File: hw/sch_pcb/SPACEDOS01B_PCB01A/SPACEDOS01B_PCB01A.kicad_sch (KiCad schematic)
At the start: 53 parts, among them M1 HOLE, M10 BMI-S-204-F, M2 HOLE, M3 HOLE, M4 HOLE, M6 BMI-S-210-F, M8 BMI-S-204-F, M9 BMI-S-204-F, U1 OPA2314, U2 OPA2314, U3 ISL21080DIH312Z-TK 1V25, U4 TS7211, U5 TS5A4594

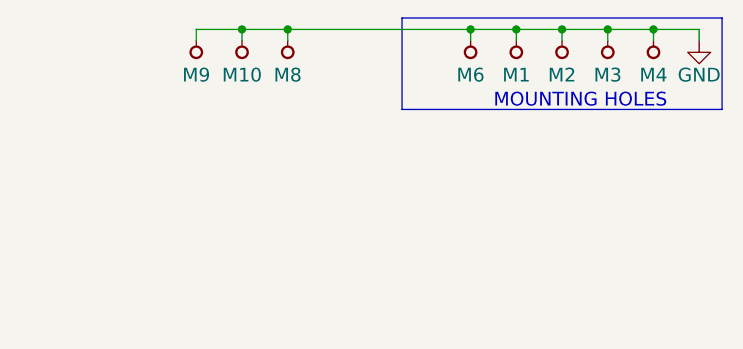
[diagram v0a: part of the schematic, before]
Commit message: Update designs to KiCAD 6. Update schematics datasheet links Minor schematics improvements (titleblocks, schematics layout)
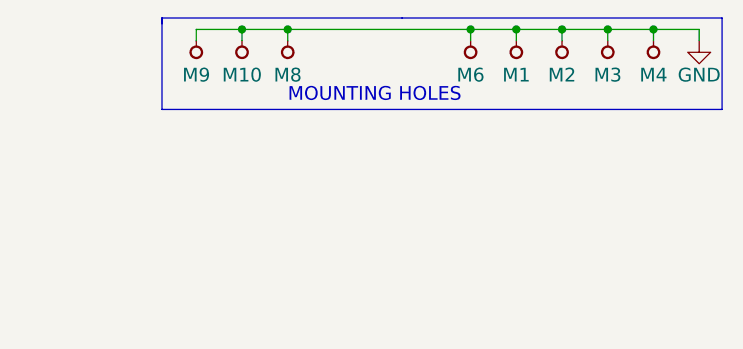
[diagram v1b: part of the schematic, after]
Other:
- company: Universal Scientific \nTechnologies s.r.o.  -> www.ust.cz
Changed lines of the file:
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@@
   (title_block
     (title "SPACEDOS01B")
-    (date "%F")
-    (company "Universal Scientific \\nTechnologies s.r.o. ")
+    (date "2023-01-26")
+    (company "www.ust.cz")
+    (comment 1 "Semiconductor \\nIonizing radiation \\nsatellite spectrometer  \\nand dosimeter ")
+    (comment 3 "Universal Scientific Technologies s.r.o. ")
   )
   (junction (at 46.99 24.13) (diameter 0) (color 0 0 0 0)
@@
     (stroke (width 0) (type default) (color 0 0 0 0))
   )
+  (polyline (pts (xy 219.71 15.24) (xy 219.71 15.875))
+    (stroke (width 0) (type default) (color 0 0 0 0))
+  )
   (wire (pts (xy 143.51 130.81) (xy 142.24 130.81))
     (stroke (width 0) (type default) (color 0 0 0 0))
@@
     (stroke (width 0) (type default) (color 0 0 0 0))
   )
-  (polyline (pts (xy 246.38 15.24) (xy 246.38 25.4))
+  (polyline (pts (xy 219.71 15.24) (xy 219.71 25.4))
     (stroke (width 0) (type default) (color 0 0 0 0))
   )
@@
     (stroke (width 0) (type default) (color 0 0 0 0))
   )
+  (polyline (pts (xy 246.38 15.24) (xy 219.71 15.24))
+    (stroke (width 0) (type default) (color 0 0 0 0))
+  )
   (wire (pts (xy 55.88 24.13) (xy 55.88 40.64))
     (stroke (width 0) (type default) (color 0 0 0 0))
@@
     (stroke (width 0) (type default) (color 0 0 0 0))
   )
+  (polyline (pts (xy 219.71 25.4) (xy 246.38 25.4))
+    (stroke (width 0) (type default) (color 0 0 0 0))
+  )
   (polyline (pts (xy 281.94 15.24) (xy 281.94 25.4))
     (stroke (width 0) (type default) (color 0 0 0 0))
@@
     (stroke (width 0) (type default) (color 0 0 0 0))
   )
-  (text "MOUNTING HOLES" (at 256.54 25.4 0)
+  (text "MOUNTING HOLES" (at 233.68 24.765 0)
     (effects (font (size 1.524 1.524)) (justify left bottom))
   )
@@
     (pin "4")
     (pin "8")
-  )
-  (symbol (lib_id "MLAB_IO:AD8692") (at 156.21 128.27 0) (mirror x) (unit 1)
-    (in_bom yes) (on_board yes)
-    (property "Reference" "U2" (id 0) (at 161.29 125.73 0)
-      (effects (font (size 1.778 1.778)) (justify left))
-    )
-    (property "Value" "OPA2314" (id 1) (at 158.75 121.92 0)
-      (effects (font (size 1.778 1.778)) (justify left))
-    )
-    (property "Footprint" "Mlab_IO:SOIC-8_3.9x4.9mm_Pitch1.27mm" (id 2) (at 156.21 128.27 0)
-      (effects (font (size 1.524 1.524)) hide)
-    )
-    (property "Datasheet" "" (id 3) (at 169.9514 125.1966 0)
-      (effects (font (size 1.524 1.524)) (justify left))
-    )
-    (pin "1")
-    (pin "2")
-    (pin "3")
-    (pin "4")
-    (pin "8")
-  )
-  (symbol (lib_id "MLAB_IO:AD8692") (at 107.95 125.73 0) (unit 2)
-    (in_bom yes) (on_board yes)
-    (property "Reference" "U1" (id 0) (at 110.49 128.27 0)
-      (effects (font (size 1.778 1.778)) (justify left))
-    )
-    (property "Value" "OPA2314" (id 1) (at 107.95 130.81 0)
-      (effects (font (size 1.778 1.778)) (justify left))
-    )
-    (property "Footprint" "Mlab_IO:SOIC-8_3.9x4.9mm_Pitch1.27mm" (id 2) (at 107.95 125.73 0)
-      (effects (font (size 1.524 1.524)) hide)
-    )
-    (property "Datasheet" "" (id 3) (at 121.6914 128.8034 0)
-      (effects (font (size 1.524 1.524)) (justify left))
-    )
     (pin "4")
     (pin "5")
@@
     (pin "8")
   )
-  (symbol (lib_id "MLAB_IO:AD8692") (at 229.87 96.52 0) (unit 2)
-    (in_bom yes) (on_board yes)
-    (property "Reference" "U2" (id 0) (at 232.41 100.33 0)
+  (symbol (lib_id "MLAB_IO:AD8692") (at 156.21 128.27 0) (mirror x) (unit 1)
+    (in_bom yes) (on_board yes)
+    (property "Reference" "U2" (id 0) (at 161.29 125.73 0)
       (effects (font (size 1.778 1.778)) (justify left))
     )
-    (property "Value" "OPA2314" (id 1) (at 229.87 102.87 0)
+    (property "Value" "OPA2314" (id 1) (at 158.75 121.92 0)
       (effects (font (size 1.778 1.778)) (justify left))
     )
-    (property "Footprint" "Mlab_IO:SOIC-8_3.9x4.9mm_Pitch1.27mm" (id 2) (at 229.87 96.52 0)
-      (effects (font (size 1.524 1.524)) hide)
-    )
-    (property "Datasheet" "" (id 3) (at 243.6114 99.5934 0)
+    (property "Footprint" "Mlab_IO:SOIC-8_3.9x4.9mm_Pitch1.27mm" (id 2) (at 156.21 128.27 0)
+      (effects (font (size 1.524 1.524)) hide)
+    )
+    (property "Datasheet" "" (id 3) (at 169.9514 125.1966 0)
       (effects (font (size 1.524 1.524)) (justify left))
     )
+    (pin "1")
+    (pin "2")
+    (pin "3")
+    (pin "4")
+    (pin "8")
     (pin "4")
     (pin "5")
@@
     (pin "8")
   )
+  (symbol (lib_id "MLAB_IO:AD8692") (at 107.95 125.73 0) (unit 2)
+    (in_bom yes) (on_board yes)
+    (property "Reference" "U1" (id 0) (at 110.49 128.27 0)
+      (effects (font (size 1.778 1.778)) (justify left))
+    )
+    (property "Value" "OPA2314" (id 1) (at 107.95 130.81 0)
+      (effects (font (size 1.778 1.778)) (justify left))
+    )
+    (property "Footprint" "Mlab_IO:SOIC-8_3.9x4.9mm_Pitch1.27mm" (id 2) (at 107.95 125.73 0)
+      (effects (font (size 1.524 1.524)) hide)
+    )
+    (property "Datasheet" "" (id 3) (at 121.6914 128.8034 0)
+      (effects (font (size 1.524 1.524)) (justify left))
+    )
+    (pin "1")
+    (pin "2")
+    (pin "3")
+    (pin "4")
+    (pin "8")
+    (pin "4")
+    (pin "5")
+    (pin "6")
+    (pin "7")
+    (pin "8")
+  )
+  (symbol (lib_id "MLAB_IO:AD8692") (at 229.87 96.52 0) (unit 2)
+    (in_bom yes) (on_board yes)
+    (property "Reference" "U2" (id 0) (at 232.41 100.33 0)
+      (effects (font (size 1.778 1.778)) (justify left))
+    )
+    (property "Value" "OPA2314" (id 1) (at 229.87 102.87 0)
+      (effects (font (size 1.778 1.778)) (justify left))
+    )
+    (property "Footprint" "Mlab_IO:SOIC-8_3.9x4.9mm_Pitch1.27mm" (id 2) (at 229.87 96.52 0)
+      (effects (font (size 1.524 1.524)) hide)
+    )
+    (property "Datasheet" "" (id 3) (at 243.6114 99.5934 0)
+      (effects (font (size 1.524 1.524)) (justify left))
+    )
+    (pin "1")
+    (pin "2")
+    (pin "3")
+    (pin "4")
+    (pin "8")
+    (pin "4")
+    (pin "5")
+    (pin "6")
+    (pin "7")
+    (pin "8")
+  )
   (symbol (lib_id "Device:C") (at 44.45 132.08 0) (unit 1)
     (in_bom yes) (on_board yes)
@@
       (effects (font (size 1.27 1.27) italic) hide)
     )
-    (property "Datasheet" "http://www.intersil.com/content/dam/Intersil/documents/fn75/fn7599.pdf" (id 3) (at 116.84 39.37 0)
+    (property "Datasheet" "https://eu.mouser.com/datasheet/2/698/REN_isl21080_DST_20040119-1998038.pdf" (id 3) (at 116.84 39.37 0)
       (effects (font (size 1.27 1.27) italic) hide)
     )

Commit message: Correcly setup automation workflows and cleanup KiCAD project.
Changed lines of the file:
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@@
+    (stroke (width 0) (type default) (color 0 0 0 0))
+  )
+  (wire (pts (xy 72.39 168.275) (xy 72.39 171.45))
     (stroke (width 0) (type default) (color 0 0 0 0))
   )
@@
     (effects (font (size 1.524 1.524)) (justify left bottom))
   )
-  (label "A/D" (at 269.24 96.52 90)
-    (effects (font (size 1.524 1.524)) (justify left bottom))
+  (label "A/D" (at 269.875 96.52 180)
+    (effects (font (size 1.524 1.524)) (justify right bottom))
   )
   (label "VCC2" (at 153.67 140.97 0)
@@
     (effects (font (size 1.524 1.524)) (justify left bottom))
   )
-  (label "VCC1" (at 92.71 24.13 0)
+  (label "VCC1" (at 85.09 24.13 0)
     (effects (font (size 1.524 1.524)) (justify left bottom))
   )
@@
     (effects (font (size 1.524 1.524)) (justify left bottom))
   )
-  (label "VCC4" (at 92.71 73.66 0)
+  (label "VCC4" (at 85.725 73.66 0)
     (effects (font (size 1.524 1.524)) (justify left bottom))
   )
@@
     (effects (font (size 1.524 1.524)) (justify left bottom))
   )
-  (label "VCC2" (at 92.71 40.64 0)
+  (label "VCC2" (at 85.725 40.64 0)
     (effects (font (size 1.524 1.524)) (justify left bottom))
   )
@@
     (effects (font (size 1.524 1.524)) (justify left bottom))
   )
-  (label "VCC3" (at 92.71 57.15 0)
+  (label "VCC3" (at 85.725 57.15 0)
     (effects (font (size 1.524 1.524)) (justify left bottom))
   )
@@
     (pin "1")
   )
+  (symbol (lib_id "power:PWR_FLAG") (at 92.71 57.15 270) (unit 1)
+    (in_bom yes) (on_board yes)
+    (property "Reference" "#FLG0108" (id 0) (at 94.615 57.15 0)
+      (effects (font (size 1.27 1.27)) hide)
+    )
+    (property "Value" "PWR_FLAG" (id 1) (at 96.52 57.15 0))
+    (property "Footprint" "" (id 2) (at 92.71 57.15 0)
+      (effects (font (size 1.27 1.27)) hide)
+    )
+    (property "Datasheet" "~" (id 3) (at 92.71 57.15 0)
+      (effects (font (size 1.27 1.27)) hide)
+    )
+    (pin "1")
+  )
+  (symbol (lib_id "power:PWR_FLAG") (at 92.71 40.64 270) (unit 1)
+    (in_bom yes) (on_board yes)
+    (property "Reference" "#FLG0106" (id 0) (at 94.615 40.64 0)
+      (effects (font (size 1.27 1.27)) hide)
+    )
+    (property "Value" "PWR_FLAG" (id 1) (at 96.52 40.64 0))
+    (property "Footprint" "" (id 2) (at 92.71 40.64 0)
+      (effects (font (size 1.27 1.27)) hide)
+    )
+    (property "Datasheet" "~" (id 3) (at 92.71 40.64 0)
+      (effects (font (size 1.27 1.27)) hide)
+    )
+    (pin "1")
+  )
+  (symbol (lib_id "power:PWR_FLAG") (at 92.71 73.66 270) (unit 1)
+    (in_bom yes) (on_board yes)
+    (property "Reference" "#FLG0107" (id 0) (at 94.615 73.66 0)
+      (effects (font (size 1.27 1.27)) hide)
+    )
+    (property "Value" "PWR_FLAG" (id 1) (at 96.52 73.66 0))
+    (property "Footprint" "" (id 2) (at 92.71 73.66 0)
+      (effects (font (size 1.27 1.27)) hide)
+    )
+    (property "Datasheet" "~" (id 3) (at 92.71 73.66 0)
+      (effects (font (size 1.27 1.27)) hide)
+    )
+    (pin "1")
+  )
+  (symbol (lib_id "power:PWR_FLAG") (at 92.71 24.13 270) (unit 1)
+    (in_bom yes) (on_board yes)
+    (property "Reference" "#FLG0104" (id 0) (at 94.615 24.13 0)
+      (effects (font (size 1.27 1.27)) hide)
+    )
+    (property "Value" "PWR_FLAG" (id 1) (at 96.52 24.13 0))
+    (property "Footprint" "" (id 2) (at 92.71 24.13 0)
+      (effects (font (size 1.27 1.27)) hide)
+    )
+    (property "Datasheet" "~" (id 3) (at 92.71 24.13 0)
+      (effects (font (size 1.27 1.27)) hide)
+    )
+    (pin "1")
+  )
+  (symbol (lib_id "power:PWR_FLAG") (at 72.39 168.275 0) (unit 1)
+    (in_bom yes) (on_board yes)
+    (property "Reference" "#FLG0103" (id 0) (at 72.39 166.37 0)
+      (effects (font (size 1.27 1.27)) hide)
+    )
+    (property "Value" "PWR_FLAG" (id 1) (at 72.39 164.465 0))
+    (property "Footprint" "" (id 2) (at 72.39 168.275 0)
+      (effects (font (size 1.27 1.27)) hide)
+    )
+    (property "Datasheet" "~" (id 3) (at 72.39 168.275 0)
+      (effects (font (size 1.27 1.27)) hide)
+    )
+    (pin "1")
+  )
   (sheet (at 171.45 20.32) (size 21.59 8.89) (fields_autoplaced)
     (stroke (width 0) (type solid) (color 0 0 0 0))
@@
   )
   (symbol_instances
+    (path "/00000000-0000-0000-0000-00005c69bcb4/ce5e6683-89d2-4848-a219-90133c45baa0"
+      (reference "#FLG0101") (unit 1) (value "PWR_FLAG") (footprint "")
+    )
+    (path "/00000000-0000-0000-0000-00005c69bcb4/1a3b6799-f683-4e10-9ee5-c0a32febcca1"
+      (reference "#FLG0102") (unit 1) (value "PWR_FLAG") (footprint "")
+    )
+    (path "/fe808d4b-cb10-4b7a-a60c-926888bb31ee"
+      (reference "#FLG0103") (unit 1) (value "PWR_FLAG") (footprint "")
+    )
+    (path "/b889ab7f-6e83-468f-9e32-4fd825f0ff56"
+      (reference "#FLG0104") (unit 1) (value "PWR_FLAG") (footprint "")
+    )
+    (path "/00000000-0000-0000-0000-00005c69bcb4/5949bfcb-3d0a-4f01-acc1-b86330bf4616"
+      (reference "#FLG0105") (unit 1) (value "PWR_FLAG") (footprint "")
+    )
+    (path "/60d76c42-1255-4f8b-a0f2-a4b6ee2da0b6"
+      (reference "#FLG0106") (unit 1) (value "PWR_FLAG") (footprint "")
+    )
+    (path "/952e743c-5d7c-40d6-9b44-e9a6cf85b9cd"
+      (reference "#FLG0107") (unit 1) (value "PWR_FLAG") (footprint "")
+    )
+    (path "/60b2a7dc-7010-4cd3-91a8-ba960734d66b"
+      (reference "#FLG0108") (unit 1) (value "PWR_FLAG") (footprint "")
+    )
+    (path "/00000000-0000-0000-0000-00005c4aedd8/2ae5a6f3-8ed4-4515-afef-fd87fb91e3e8"
+      (reference "#FLG0109") (unit 1) (value "PWR_FLAG") (footprint "")
+    )
     (path "/00000000-0000-0000-0000-00005b3d3f19"
       (reference "#PWR03") (unit 1) (value "GND") (footprint "")
